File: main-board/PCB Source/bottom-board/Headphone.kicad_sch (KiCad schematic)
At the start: 29 parts, among them P14 AudioJack3, Q10 MMBFJ110, Q9 MMBFJ110, U8 LM4811

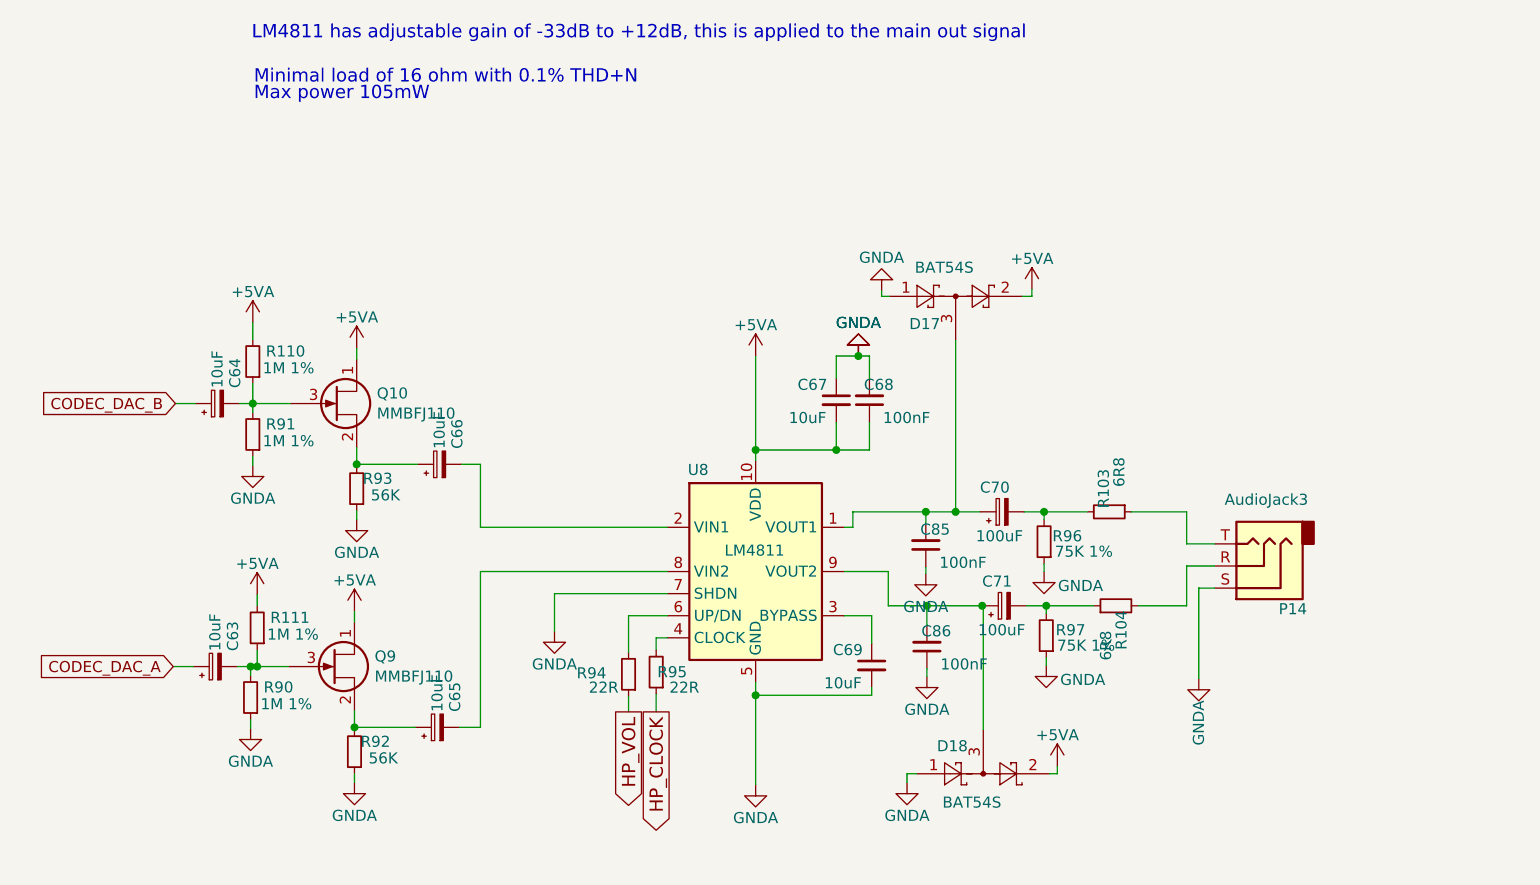
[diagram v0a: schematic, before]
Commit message: mainboard: add bias buffer, update MPNs, clean schematic
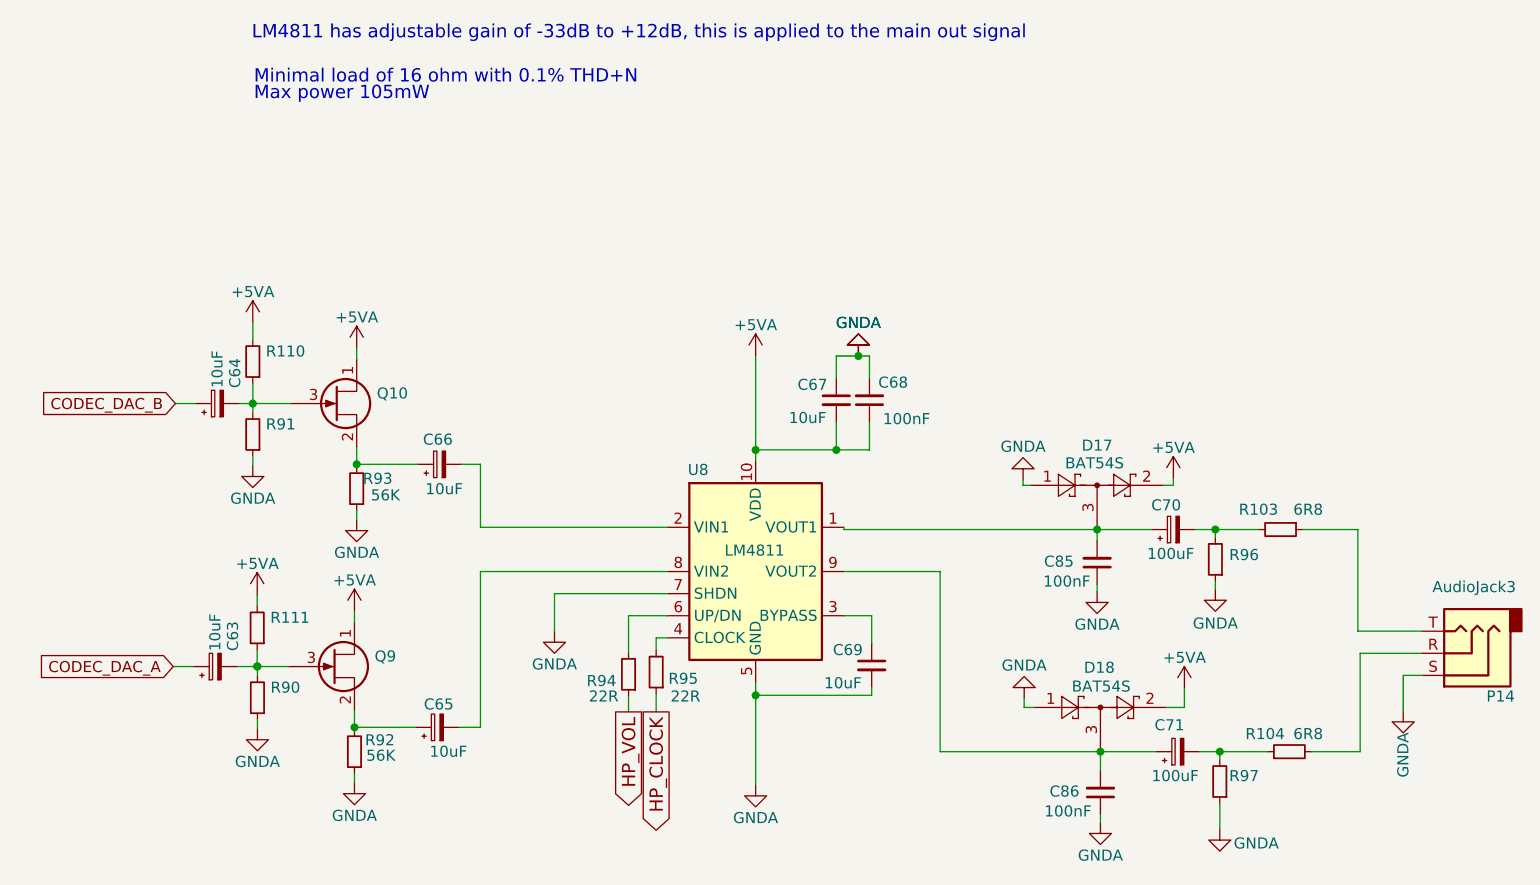
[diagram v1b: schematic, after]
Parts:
- Q10, Q9: value MMBFJ110 -> (none); footprint Package_TO_SOT_SMD:SOT-23 -> (none); MPN MMBFJ110 -> MMBFJ211CT-ND
- R110, R111, R90, R91: value 1M 1% -> (none); footprint Resistor_SMD:R_0603_1608Metric -> (none)
- R96: value 75K 1% -> (none); footprint Resistor_SMD:R_0603_1608Metric -> (none)
- R97: value 75K 1% -> (none)
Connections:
- net at C63.2, Q9.3 (G), R111.1: no longer R90.2
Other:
- moved on the sheet: C70, C71, C85, C86, D17, D18, P14, R103, R104, R90, R96, R97

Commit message: mainboard: modify silkscreen
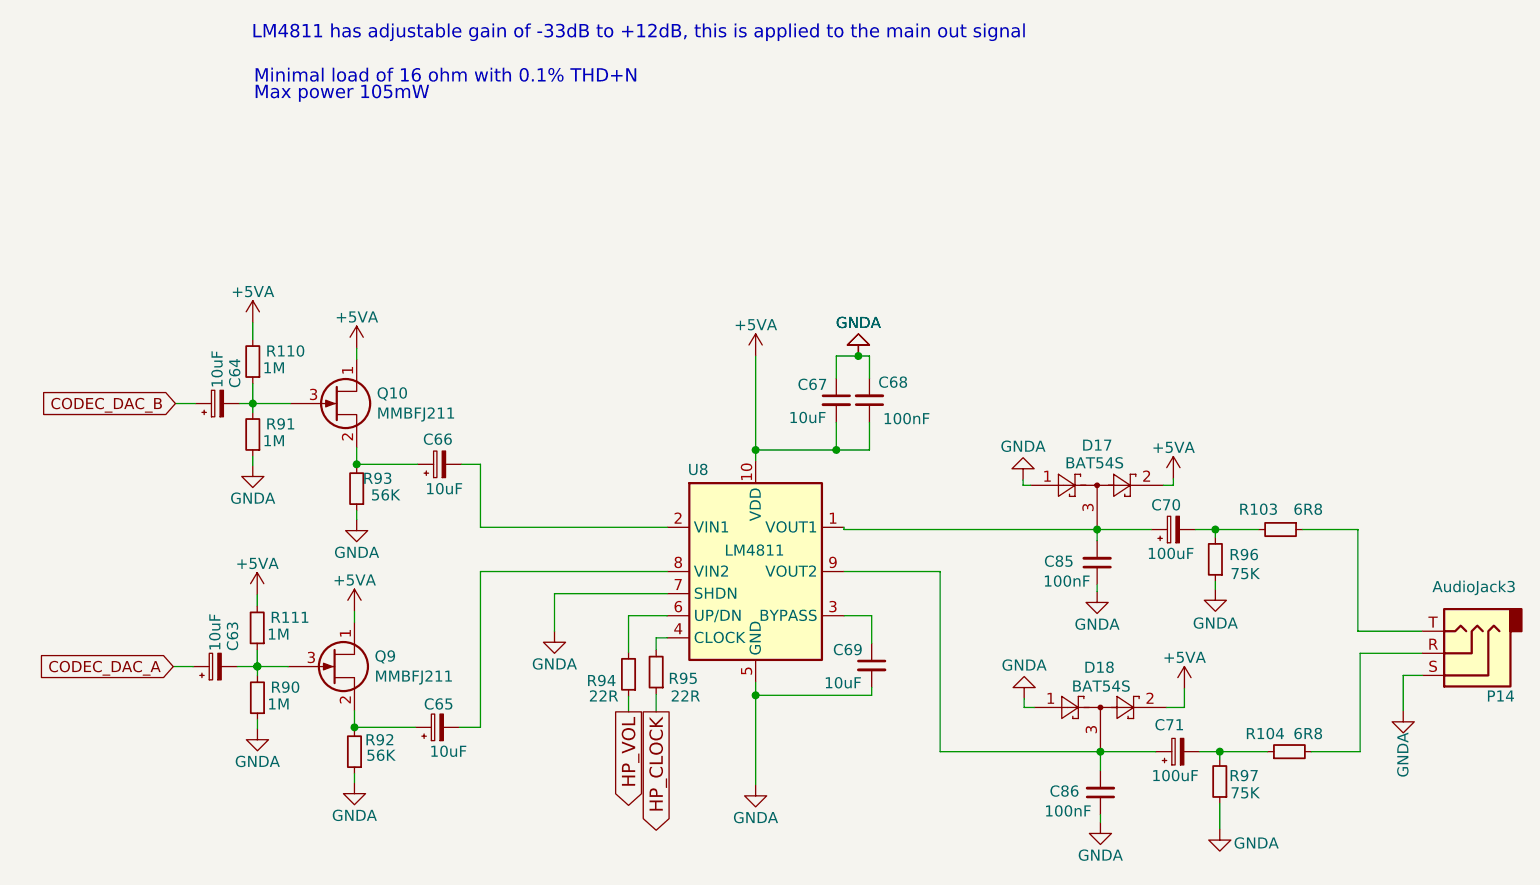
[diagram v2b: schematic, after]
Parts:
- Q10, Q9: value (none) -> MMBFJ211; footprint (none) -> Package_TO_SOT_SMD:SOT-23
- R110, R111, R90, R91: value (none) -> 1M; footprint (none) -> Resistor_SMD:R_0603_1608Metric
- R96: value (none) -> 75K; footprint (none) -> Resistor_SMD:R_0603_1608Metric
- R97: value (none) -> 75K
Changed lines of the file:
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@@
       (effects (font (size 1.27 1.27)) (justify left))
     )
-    (property "Value" "" (id 1) (at 103.0224 77.978 0)
-      (effects (font (size 1.27 1.27)) (justify left))
-    )
-    (property "Footprint" "" (id 2) (at 103.251 74.295 0)
+    (property "Value" "MMBFJ211" (id 1) (at 103.0224 77.978 0)
+      (effects (font (size 1.27 1.27)) (justify left))
+    )
+    (property "Footprint" "Package_TO_SOT_SMD:SOT-23" (id 2) (at 103.251 74.295 0)
       (effects (font (size 1.27 1.27)) hide)
     )
@@
       (effects (font (size 1.27 1.27)) (justify right))
     )
-    (property "Value" "" (id 1) (at 89.916 81.153 0)
-      (effects (font (size 1.27 1.27)) (justify right))
-    )
-    (property "Footprint" "" (id 2) (at 88.773 80.391 0)
+    (property "Value" "1M" (id 1) (at 89.916 81.153 0)
+      (effects (font (size 1.27 1.27)) (justify right))
+    )
+    (property "Footprint" "Resistor_SMD:R_0603_1608Metric" (id 2) (at 88.773 80.391 0)
       (effects (font (size 1.27 1.27)) hide)
     )
@@
       (effects (font (size 1.27 1.27)) (justify left))
     )
-    (property "Value" "" (id 1) (at 102.7684 108.204 0)
-      (effects (font (size 1.27 1.27)) (justify left))
-    )
-    (property "Footprint" "" (id 2) (at 102.997 104.521 0)
+    (property "Value" "MMBFJ211" (id 1) (at 102.7684 108.204 0)
+      (effects (font (size 1.27 1.27)) (justify left))
+    )
+    (property "Footprint" "Package_TO_SOT_SMD:SOT-23" (id 2) (at 102.997 104.521 0)
       (effects (font (size 1.27 1.27)) hide)
     )
@@
       (effects (font (size 1.27 1.27)) (justify right))
     )
-    (property "Value" "" (id 1) (at 90.4494 111.4044 0)
-      (effects (font (size 1.27 1.27)) (justify right))
-    )
-    (property "Footprint" "" (id 2) (at 89.3064 110.6424 0)
+    (property "Value" "1M" (id 1) (at 90.4494 111.4044 0)
+      (effects (font (size 1.27 1.27)) (justify right))
+    )
+    (property "Footprint" "Resistor_SMD:R_0603_1608Metric" (id 2) (at 89.3064 110.6424 0)
       (effects (font (size 1.27 1.27)) hide)
     )
@@
     (in_bom yes) (on_board yes)
     (property "Reference" "R96" (id 0) (at 202.692 94.234 0))
-    (property "Value" "" (id 1) (at 202.7936 96.4184 0))
-    (property "Footprint" "" (id 2) (at 199.39 94.742 0)
+    (property "Value" "75K" (id 1) (at 202.7936 96.4184 0))
+    (property "Footprint" "Resistor_SMD:R_0603_1608Metric" (id 2) (at 199.39 94.742 0)
       (effects (font (size 1.27 1.27)) hide)
     )
@@
     (in_bom yes) (on_board yes)
     (property "Reference" "R97" (id 0) (at 202.692 119.634 0))
-    (property "Value" "" (id 1) (at 202.7936 121.6152 0))
+    (property "Value" "75K" (id 1) (at 202.7936 121.6152 0))
     (property "Footprint" "Resistor_SMD:R_0603_1608Metric" (id 2) (at 199.898 120.269 0)
       (effects (font (size 1.27 1.27)) hide)
@@
       (effects (font (size 1.27 1.27)) (justify right))
     )
-    (property "Value" "" (id 1) (at 89.916 72.771 0)
-      (effects (font (size 1.27 1.27)) (justify right))
-    )
-    (property "Footprint" "" (id 2) (at 88.773 72.009 0)
+    (property "Value" "1M" (id 1) (at 89.916 72.771 0)
+      (effects (font (size 1.27 1.27)) (justify right))
+    )
+    (property "Footprint" "Resistor_SMD:R_0603_1608Metric" (id 2) (at 88.773 72.009 0)
       (effects (font (size 1.27 1.27)) hide)
     )
@@
       (effects (font (size 1.27 1.27)) (justify right))
     )
-    (property "Value" "" (id 1) (at 90.424 103.378 0)
-      (effects (font (size 1.27 1.27)) (justify right))
-    )
-    (property "Footprint" "" (id 2) (at 89.281 102.616 0)
-      (effects (font (size 1.27 1.27)) hide)
-    )
+    (property "Value" "1M" (id 1) (at 90.424 103.378 0)
+      (effects (font (size 1.27 1.27)) (justify right))
+    )
+    (property "Footprint" "Resistor_SMD:R_0603_1608Metric" (id 2) (at 89.281 102.616 0)
+      (effects (font (size 1.27 1.27)) hide)
+    )
